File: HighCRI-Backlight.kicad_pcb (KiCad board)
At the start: 2 copper layers, 100 x 100 mm, 120 parts, among them J1 Conn_01x03, J2 Screw_Terminal_01x02, J3 Screw_Terminal_01x02, Q1 AOD4130, Q2 AOD4130, Q3 AOD4130, U1 L78L24_SO8, U2 LM324

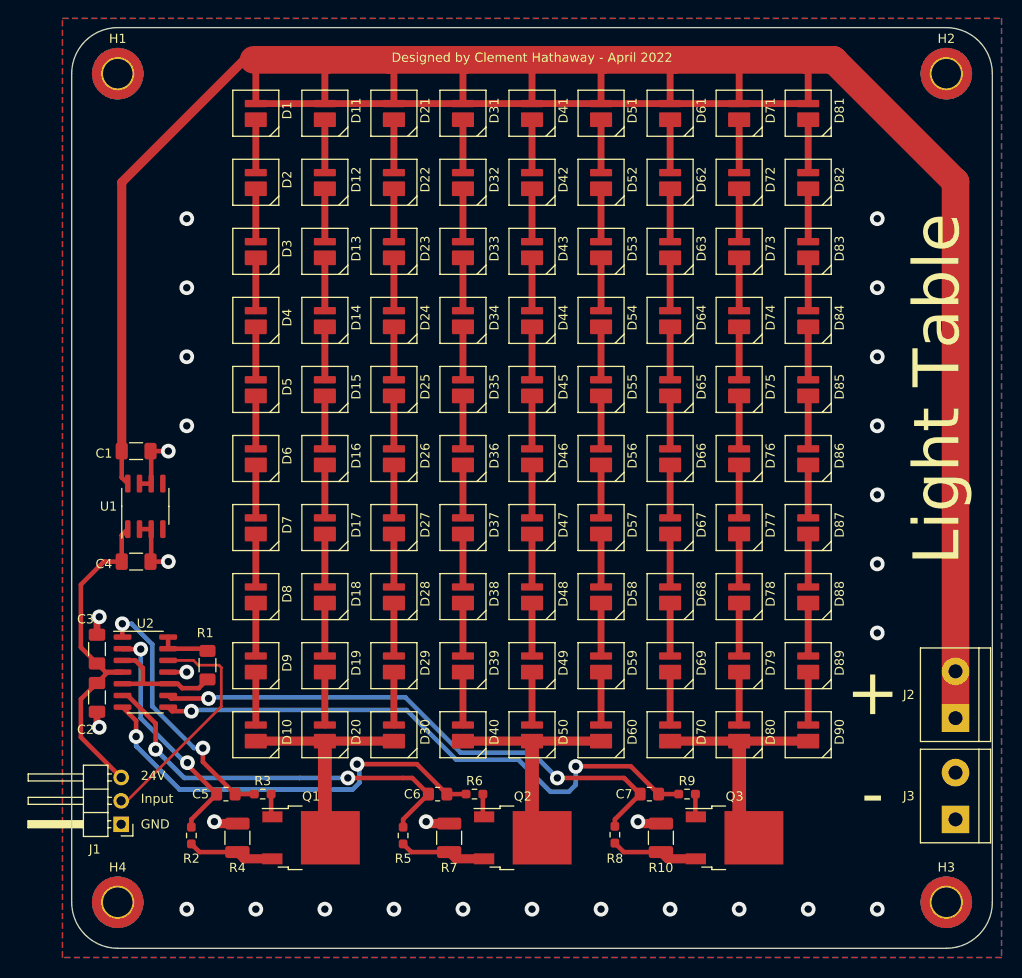
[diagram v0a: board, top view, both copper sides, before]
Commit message: Finished Single Sided Design
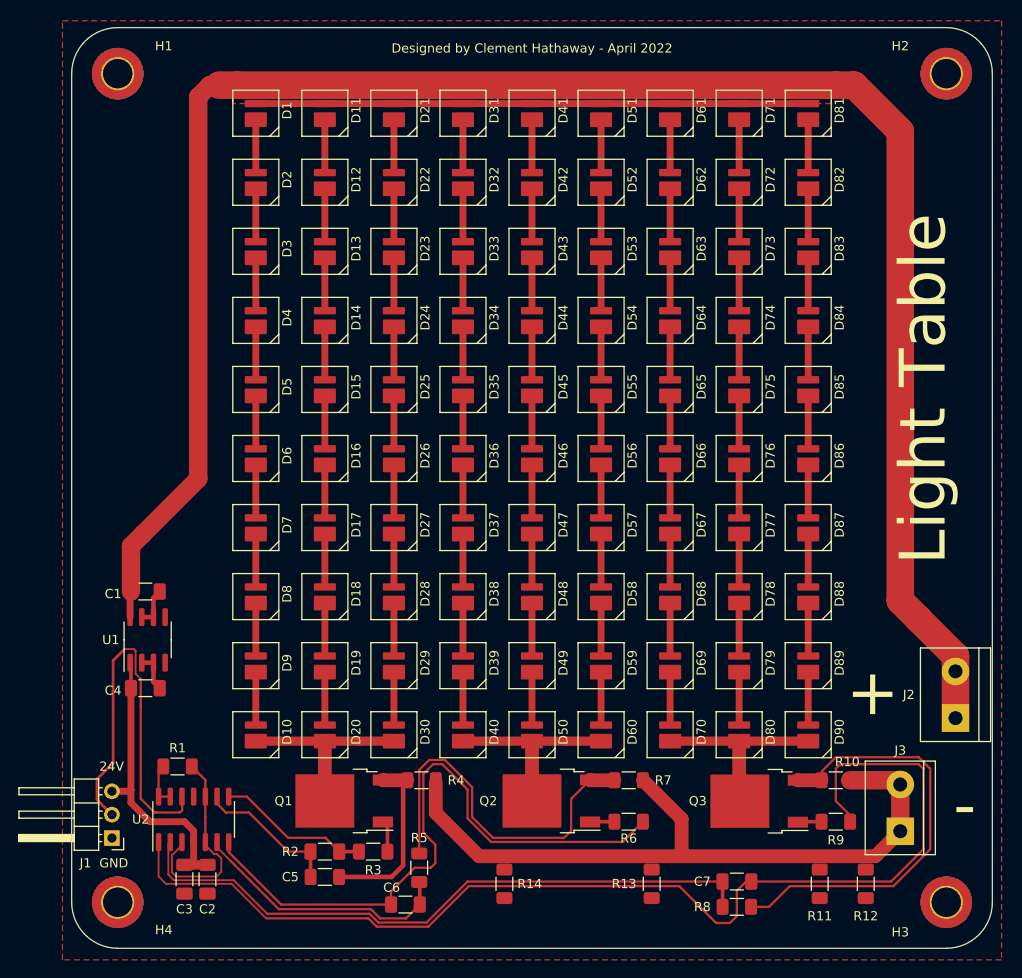
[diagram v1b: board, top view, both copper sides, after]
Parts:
- removed G***: LOGO, LOGO
- added R11: 0R, Resistor_SMD:R_1206_3216Metric_Pad1.30x1.75mm_HandSolder, F.Cu at (187.0, 140.2)
- added R12: 0R, Resistor_SMD:R_1206_3216Metric_Pad1.30x1.75mm_HandSolder, F.Cu at (192.0, 140.2)
- added R13: 0R, Resistor_SMD:R_1206_3216Metric_Pad1.30x1.75mm_HandSolder, F.Cu at (168.8, 140.2)
- added R14: 0R, Resistor_SMD:R_1206_3216Metric_Pad1.30x1.75mm_HandSolder, F.Cu at (152.8, 140.2)
- C5, C6, C7: footprint Resistor_SMD:R_0805_2012Metric_Pad1.20x1.40mm_HandSolder -> Capacitor_SMD:C_1206_3216Metric_Pad1.33x1.80mm_HandSolder
- R10, R4, R7: footprint Resistor_SMD:R_1210_3225Metric_Pad1.30x2.65mm_HandSolder -> Resistor_SMD:R_1206_3216Metric_Pad1.30x1.75mm_HandSolder
- R2, R3, R5, R6, R8, R9: footprint Resistor_SMD:R_0603_1608Metric_Pad0.98x0.95mm_HandSolder -> Resistor_SMD:R_1206_3216Metric_Pad1.30x1.75mm_HandSolder
- moved C3 26.7 mm to (118.0, 139.8), turned to -90 degrees
- moved C2 23.1 mm to (120.5, 139.8)
- moved R4 21.0 mm to (143.8, 129.0), turned to 0 degrees
- moved R7 20.5 mm to (166.2, 129.0), turned to 0 degrees
- moved R10 20.0 mm to (188.8, 129.0), turned to 0 degrees
- moved R6 17.0 mm to (166.2, 133.5), turned to 180 degrees
- moved U2 16.8 mm to (119.0, 133.2), turned to 90 degrees
- moved R9 16.4 mm to (188.8, 133.5), turned to 180 degrees
- moved R8 15.4 mm to (178.0, 142.8), turned to 0 degrees
- moved C1 15.3 mm to (113.8, 108.5)
- moved R2 15.2 mm to (133.2, 139.5), turned to 0 degrees
- moved U1 14.5 mm to (114.0, 113.8)
- moved C4 13.8 mm to (113.8, 119.0)
- moved R3 13.5 mm to (138.5, 136.8)
- moved C7 13.4 mm to (178.0, 140.0)
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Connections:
- U2 pad 1: Net-(C5-Pad1) -> Net-(C7-Pad1)
- U2 pad 2: Net-(C5-Pad2) -> Net-(C7-Pad2)
- U2 pad 8: Net-(C7-Pad1) -> Net-(C5-Pad1)
- U2 pad 9: Net-(C7-Pad2) -> Net-(C5-Pad2)
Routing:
- net Net-(C7-Pad1): track 62.9 -> 122.5 mm, vias 2 -> 0
- net GND: track 27.1 -> 86.7 mm, vias 30 -> 0
- net Net-(Q3-Pad3): track 9.51 -> 47.8 mm
- net +36V: track 296.5 -> 264.7 mm
- net Net-(Q2-Pad3): track 9.47 -> 40.8 mm
- net Net-(C6-Pad1): track 46.6 -> 69.4 mm, vias 2 -> 0
- net Net-(J1-Pad2): track 25.5 -> 44.2 mm
- net Net-(C6-Pad2): track 44.0 -> 28.9 mm, vias 2 -> 0
- net Net-(C5-Pad1): track 28.3 -> 16.6 mm, vias 2 -> 0
- net Net-(C5-Pad2): track 26.0 -> 15.8 mm, vias 2 -> 0
- net Net-(C7-Pad2): track 60.4 -> 70.6 mm, vias 2 -> 0
- net Net-(Q1-Pad3): track 9.47 -> 19.6 mm
- net /I_SET: track 14.1 -> 22.4 mm
- net +24V: track 37.8 -> 31.8 mm
- net Net-(D70-Pad1): track 26.2 -> 21.6 mm
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- added copper zone on F.Cu, net +36V
- removed copper zone on B.Cu, net GND
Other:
- board text removed: "Input"

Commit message: Minor errors
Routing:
- net +36V: track 264.7 -> 285.2 mm

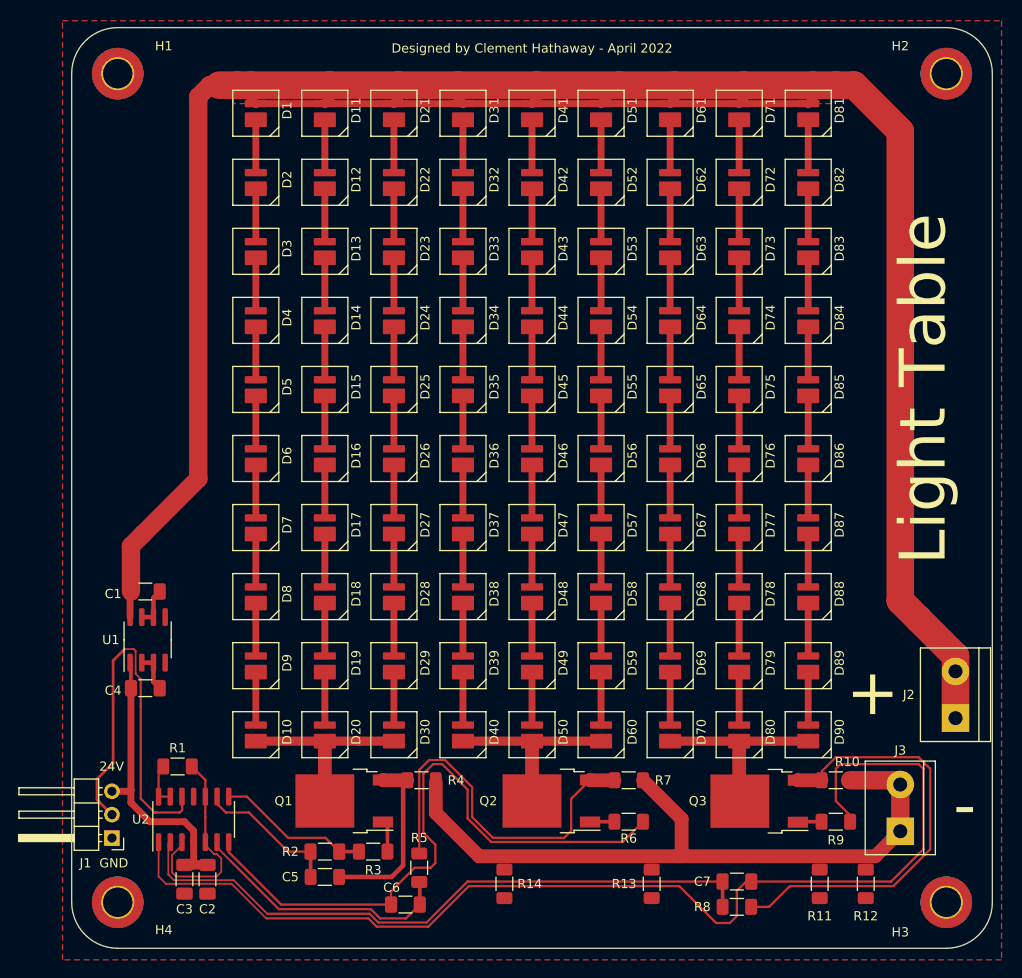
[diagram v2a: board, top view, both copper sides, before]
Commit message: Fixed some things
KiCAD still glitching on jumper resistors
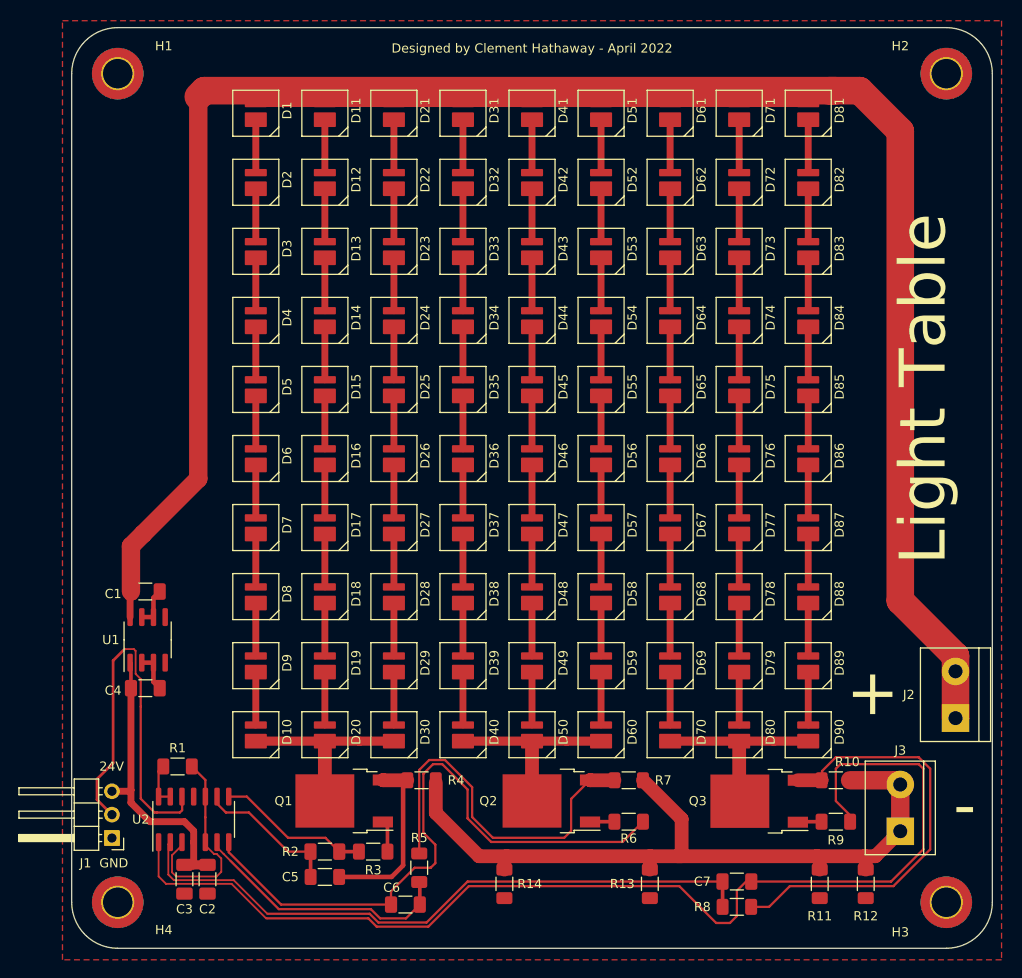
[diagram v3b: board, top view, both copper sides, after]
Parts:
- moved R13 0.20 mm to (168.6, 140.2)
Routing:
- net +36V: track 285.2 -> 275.5 mm
- net GND: track 86.7 -> 92.8 mm
- net Net-(Q3-Pad3): track 47.8 -> 47.3 mm
- removed copper zone on F.Cu, net +36V
